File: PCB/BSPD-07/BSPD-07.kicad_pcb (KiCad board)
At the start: 2 copper layers, 32 x 70.9 mm, 54 parts, among them IC1 LM393LVQDRQ1, IC2 LM393LVQDRQ1, IC3 LM393LVQDRQ1, IC4 LDO40LPU50RY, IC5 74LVC1G02GW-Q100H, J1 DTM13-12PA, Q1 RSQ025P03HZGTR, Q2 RJU002N06FRAT106, Q3 RJU002N06FRAT106, U2 TLP175A / COMUS AB38-Q

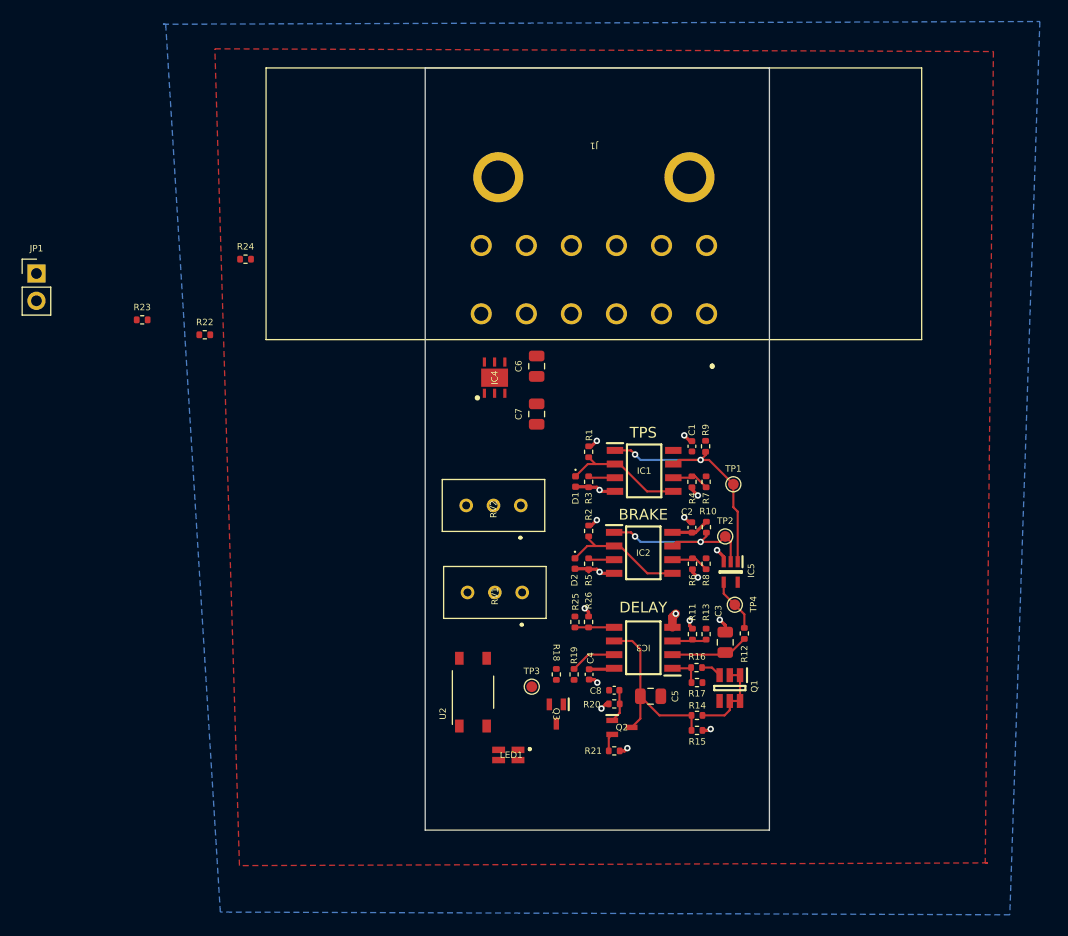
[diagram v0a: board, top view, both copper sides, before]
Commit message: Finished PCB layout
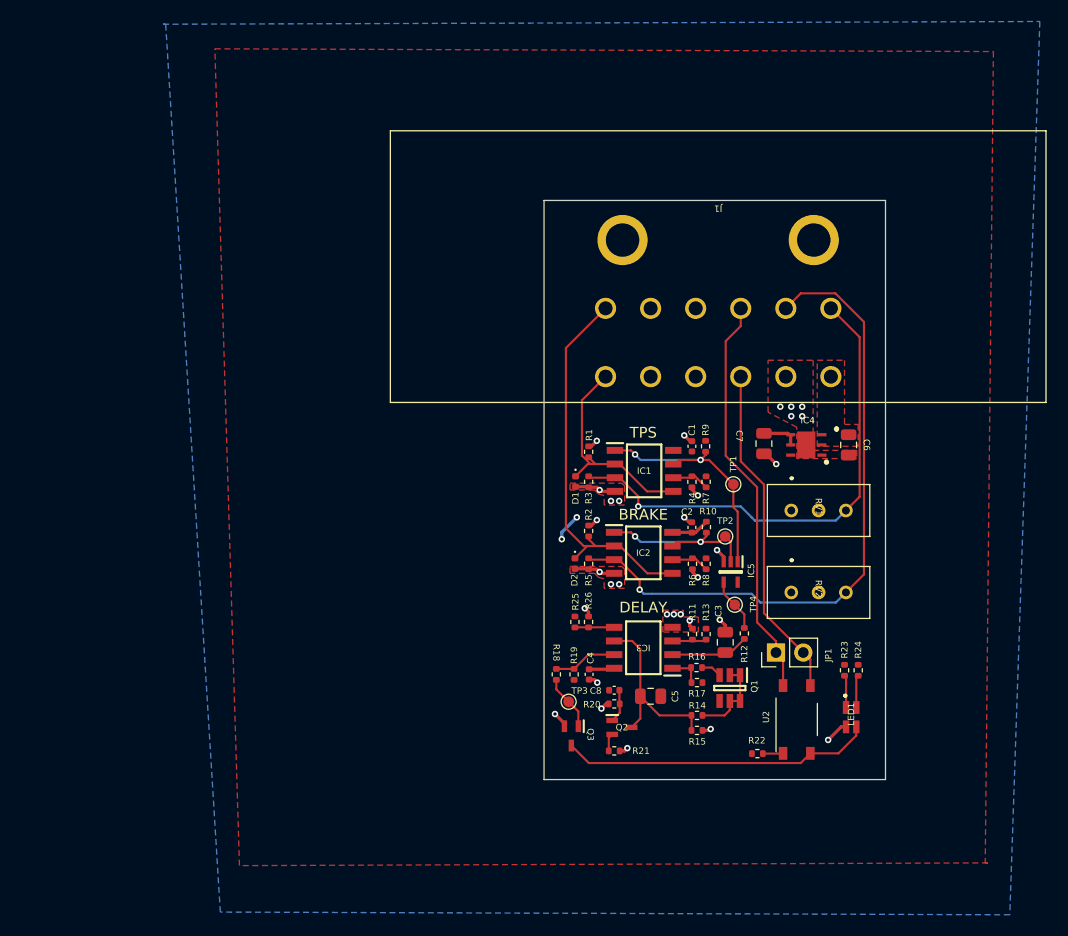
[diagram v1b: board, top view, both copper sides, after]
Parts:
- moved JP1 77.3 mm to (169.4, 124.5), turned to 90 degrees
- moved R23 73.0 mm to (175.7, 126.1), turned to 90 degrees
- moved R24 68.6 mm to (177.0, 126.1), turned to 90 degrees
- moved R22 64.5 mm to (167.6, 133.9), turned to 180 degrees
- moved LED1 32.1 mm to (176.4, 130.5), turned to 90 degrees
- moved RV2 31.3 mm to (173.3, 118.9), turned to -90 degrees
- moved RV1 31.0 mm to (173.3, 111.3), turned to -90 degrees
- moved U2 30.2 mm to (171.3, 130.7)
- moved C6 29.9 mm to (176.1, 105.2), turned to -90 degrees
- moved IC4 29.6 mm to (172.2, 105.2), turned to 180 degrees
- moved C7 21.3 mm to (168.2, 105.1), turned to -90 degrees
- moved J1 12.9 mm to (174.5, 98.8)
- moved TP3 3.70 mm to (150.1, 129.1)
- moved Q3 2.47 mm to (150.3, 132.2)
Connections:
- J1 pad 10: unconnected-(J1-Pad10) -> SAFETY_IN
- J1 pad 11: BRAKE_IN -> BRAKE_TRIG
- J1 pad 12: TPS_IN -> TPS_TRIG
- J1 pad 3: unconnected-(J1-Pad3) -> SAFETY_OUT
- J1 pad 5: SAFETY_IN -> +5V
- J1 pad 6: SAFETY_OUT -> TPS_IN
- J1 pad 7: TPS_TRIG -> BRAKE_IN
- J1 pad 8: BRAKE_TRIG -> unconnected-(J1-Pad8)
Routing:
- net BRAKE_TRIG: track 2.42 -> 61.3 mm, vias 0 -> 1
- net TPS_TRIG: track 2.71 -> 47.0 mm, vias 0 -> 1
- net SAFETY_IN: track 0.00 -> 37.9 mm
- net SAFETY_OUT: track 0.00 -> 31.4 mm
- net INFO_LED: track 0.00 -> 29.0 mm
- net BRAKE_IN: track 11.7 -> 36.4 mm
- net TPS_IN: track 11.7 -> 20.9 mm
- net +5V: track 5.95 -> 12.0 mm, vias 0 -> 2
- net ERR_FINAL: track 0.00 -> 5.15 mm
- net GND: track 23.2 -> 26.5 mm, vias 17 -> 31
- net Net-(LED1-Pad4): track 0.00 -> 3.02 mm
- net Net-(LED1-Pad1): track 0.00 -> 3.01 mm
- net Net-(R22-Pad1): track 0.00 -> 1.89 mm
- net Net-(IC3-Pad7): track 4.27 -> 5.92 mm
- added copper zone on F.Cu, net +12V
- added copper zone on F.Cu, net GND
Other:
- board size 32 x 70.9 mm -> 31.8 x 53.8 mm

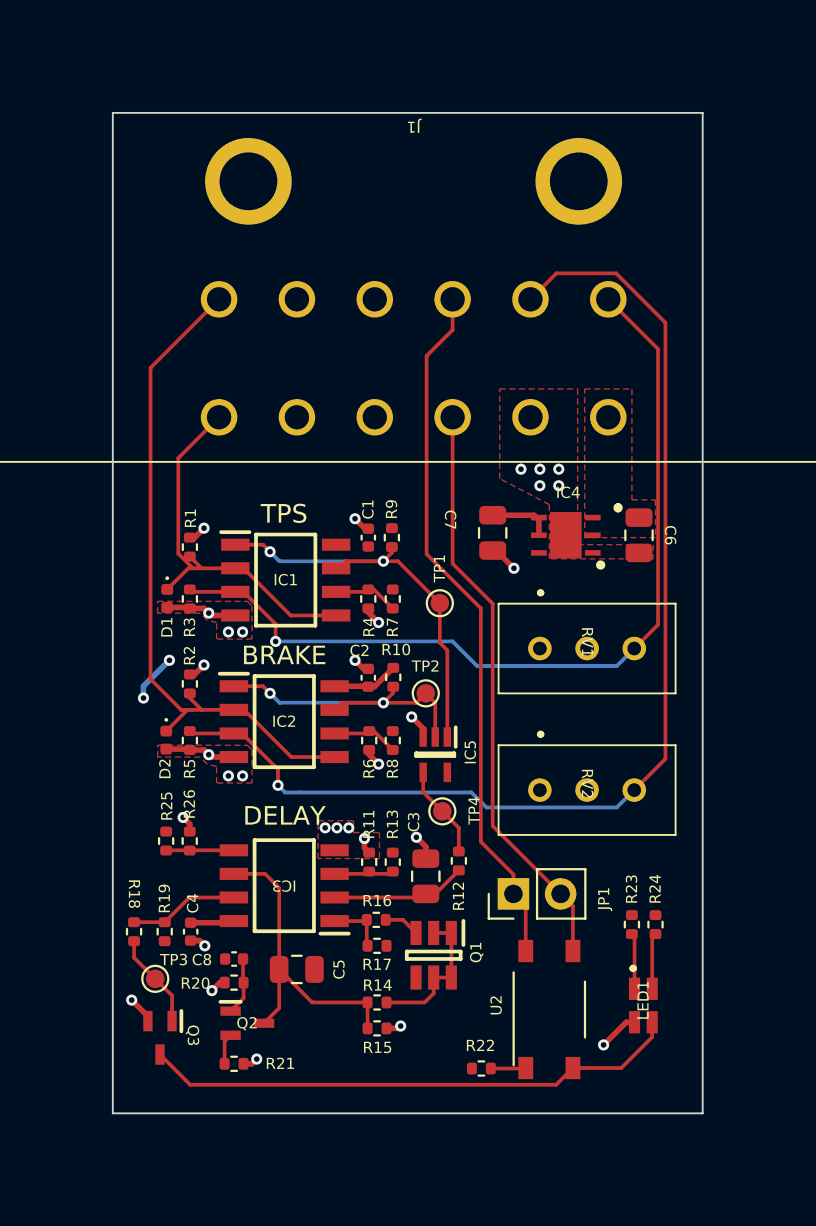
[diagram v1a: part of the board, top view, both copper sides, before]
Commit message: Rounded corners
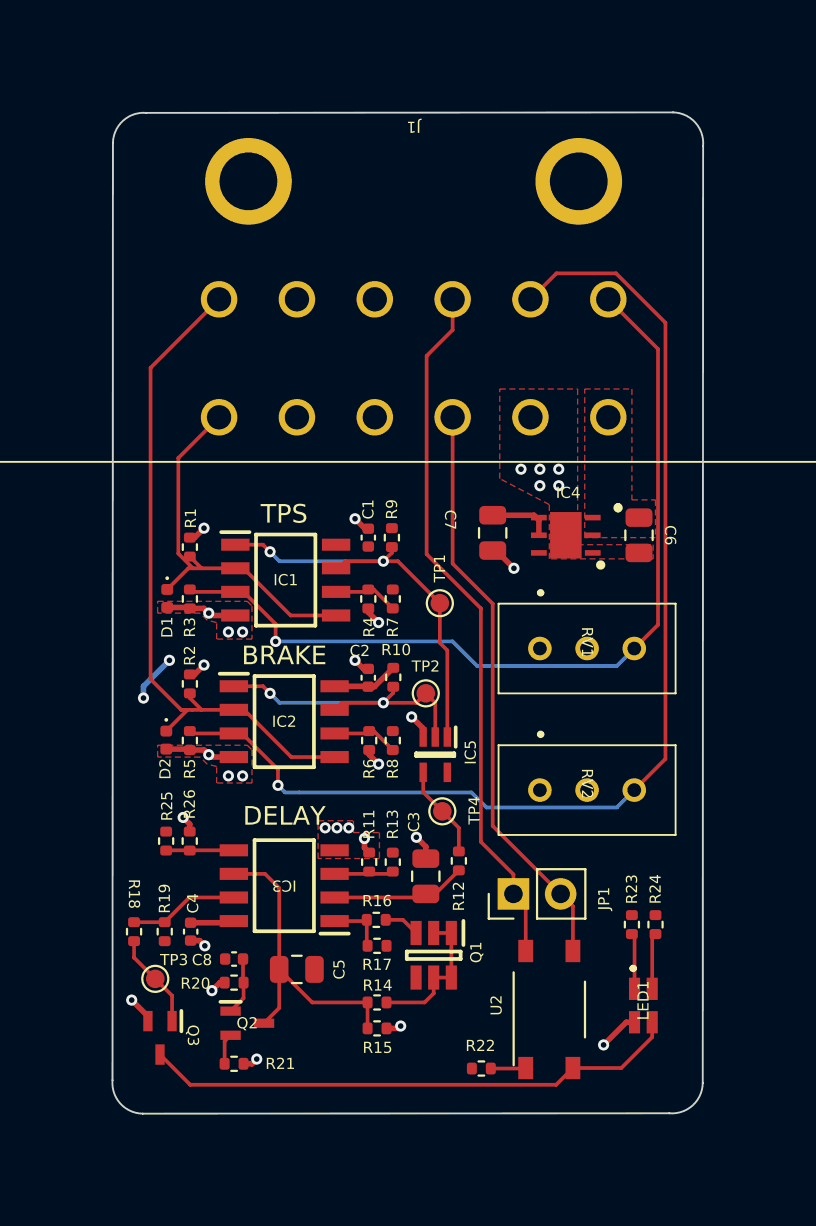
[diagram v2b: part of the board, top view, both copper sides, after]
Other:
- board size 31.8 x 53.8 mm -> 31.8 x 53.9 mm
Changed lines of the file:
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@@
     )
   )
-  (gr_rect (start 147.7998 82.4484) (end 179.5498 136.2964) (layer "Edge.Cuts") (width 0.1) (fill none))
+  (gr_arc (start 177.946443 82.421253) (mid 179.1528 82.9674) (end 179.571928 84.223547) (layer "Edge.Cuts") (width 0.1))
+  (gr_line (start 149.608947 82.448272) (end 177.946443 82.421253) (layer "Edge.Cuts") (width 0.1))
+  (gr_arc (start 179.5528 134.6674) (mid 179.006653 135.873757) (end 177.750506 136.292885) (layer "Edge.Cuts") (width 0.1))
+  (gr_arc (start 147.806653 84.073757) (mid 148.3528 82.8674) (end 149.608947 82.448272) (layer "Edge.Cuts") (width 0.1))
+  (gr_line (start 179.571928 84.223547) (end 179.5528 134.6674) (layer "Edge.Cuts") (width 0.1))
+  (gr_line (start 147.783672 134.511253) (end 147.806653 84.073757) (layer "Edge.Cuts") (width 0.1))
+  (gr_line (start 149.409157 136.313547) (end 177.750506 136.292885) (layer "Edge.Cuts") (width 0.1))
+  (gr_arc (start 149.409157 136.313547) (mid 148.2028 135.7674) (end 147.783672 134.511253) (layer "Edge.Cuts") (width 0.1))
   (gr_text "DELAY" (at 157.0268 120.2944) (layer "F.SilkS")
     (effects (font (size 1 1) (thickness 0.15)))

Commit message: Tinkle of a rose petal ;)
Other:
- board text added: "12V"
- board text added: "5V"
- board text added: "BRK_IN"
- board text added: "BRK_TRIG"
- board text added: "BSPD - FSG 2023"
- board text added: "GND"
- board text added: "SF_IN"
- board text added: "SF_OUT"
- board text added: "TPS_IN"
- board text added: "TPS_TRIG"
- board text added: "by K.Pergol"
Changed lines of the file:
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@@
   (net 34 "/10s REF")
   (net 35 "/10ms VAL")
-  (net 36 "Net-(R6-Pad2)")
+  (net 36 "Net-(IC2-Pad6)")
   (net 37 "unconnected-(J1-Pad8)")
   (footprint "TestPoint:TestPoint_Pad_D1.0mm" (layer "F.Cu")
@@
       (net 7 "BRAKE_IN") (pinfunction "IN2+") (pintype "passive"))
     (pad "6" smd rect (at 2.711 0.635 90) (size 0.65 1.528) (layers "F.Cu" "F.Paste" "F.Mask")
-      (net 36 "Net-(R6-Pad2)") (pinfunction "IN2-") (pintype "passive"))
+      (net 36 "Net-(IC2-Pad6)") (pinfunction "IN2-") (pintype "passive"))
     (pad "7" smd rect (at 2.711 -0.635 90) (size 0.65 1.528) (layers "F.Cu" "F.Paste" "F.Mask")
       (net 6 "BRAKE_COMP_OUT") (pinfunction "OUT2") (pintype "passive"))
@@
     (fp_line (start 0.525 0.27) (end -0.525 0.27) (layer "F.Fab") (width 0.1))
     (pad "1" smd roundrect (at -0.51 0 90) (size 0.54 0.64) (layers "F.Cu" "F.Paste" "F.Mask") (roundrect_rratio 0.25)
-      (net 36 "Net-(R6-Pad2)") (pintype "passive"))
+      (net 36 "Net-(IC2-Pad6)") (pintype "passive"))
     (pad "2" smd roundrect (at 0.51 0 90) (size 0.54 0.64) (layers "F.Cu" "F.Paste" "F.Mask") (roundrect_rratio 0.25)
       (net 5 "+5V") (pintype "passive"))
@@
       (net 3 "GND") (pintype "passive"))
     (pad "2" smd roundrect (at 0.51 0 90) (size 0.54 0.64) (layers "F.Cu" "F.Paste" "F.Mask") (roundrect_rratio 0.25)
-      (net 36 "Net-(R6-Pad2)") (pintype "passive"))
+      (net 36 "Net-(IC2-Pad6)") (pintype "passive"))
     (model "${KICAD6_3DMODEL_DIR}/Resistor_SMD.3dshapes/R_0402_1005Metric.wrl"
       (offset (xyz 0 0 0))
@@
       (net 7 "BRAKE_IN") (pinfunction "7") (pintype "passive"))
     (pad "8" thru_hole circle (at 16.76 6.35 180) (size 1.965 1.965) (drill 1.31) (layers *.Cu *.Mask)
-      (net 37 "unconnected-(J1-Pad8)") (pinfunction "8") (pintype "passive"))
+      (net 37 "unconnected-(J1-Pad8)") (pinfunction "8") (pintype "passive+no_connect"))
     (pad "9" thru_hole circle (at 12.57 6.35 180) (size 1.965 1.965) (drill 1.31) (layers *.Cu *.Mask)
       (net 12 "unconnected-(J1-Pad9)") (pinfunction "9") (pintype "passive+no_connect"))
@@
   (gr_line (start 149.409157 136.313547) (end 177.750506 136.292885) (layer "Edge.Cuts") (width 0.1))
   (gr_arc (start 149.409157 136.313547) (mid 148.2028 135.7674) (end 147.783672 134.511253) (layer "Edge.Cuts") (width 0.1))
+  (gr_text "BRK_IN" (at 153.5148 94.5134) (layer "B.SilkS")
+    (effects (font (size 0.6 0.6) (thickness 0.15)) (justify mirror))
+  )
+  (gr_text "BRK_TRIG" (at 170.0248 94.2594) (layer "B.SilkS")
+    (effects (font (size 0.6 0.6) (thickness 0.15)) (justify mirror))
+  )
+  (gr_text "by K.Pergol" (at 149.1968 109.7534 -90) (layer "B.SilkS")
+    (effects (font (size 0.9 0.9) (thickness 0.15)) (justify mirror))
+  )
+  (gr_text "12V" (at 174.5968 100.6094) (layer "B.SilkS")
+    (effects (font (size 0.6 0.6) (thickness 0.15)) (justify mirror))
+  )
+  (gr_text "TPS_IN" (at 153.5148 100.8634) (layer "B.SilkS")
+    (effects (font (size 0.6 0.6) (thickness 0.15)) (justify mirror))
+  )
+  (gr_text "SF_OUT" (at 165.9608 100.6094) (layer "B.SilkS")
+    (effects (font (size 0.6 0.6) (thickness 0.15)) (justify mirror))
+  )
+  (gr_text "BSPD - FSG 2023" (at 151.7368 119.4054 -90) (layer "B.SilkS")
+    (effects (font (size 2 2) (thickness 0.15)) (justify mirror))
+  )
+  (gr_text "SF_IN" (at 165.9608 94.2594) (layer "B.SilkS")
+    (effects (font (size 0.6 0.6) (thickness 0.15)) (justify mirror))
+  )
+  (gr_text "TPS_TRIG" (at 174.3428 94.2594) (layer "B.SilkS")
+    (effects (font (size 0.6 0.6) (thickness 0.15)) (justify mirror))
+  )
+  (gr_text "5V" (at 157.5788 100.8634) (layer "B.SilkS")
+    (effects (font (size 0.6 0.6) (thickness 0.15)) (justify mirror))
+  )
+  (gr_text "GND" (at 170.5328 100.6094) (layer "B.SilkS")
+    (effects (font (size 0.6 0.6) (thickness 0.15)) (justify mirror))
+  )
   (gr_text "DELAY" (at 157.0268 120.2944) (layer "F.SilkS")
     (effects (font (size 1 1) (thickness 0.15)))
